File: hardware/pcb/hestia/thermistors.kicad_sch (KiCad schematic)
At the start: 62 parts, among them J10 B2B-ZR, J11 B2B-ZR, J12 B2B-ZR, J13 B2B-ZR, J14 B2B-ZR, J15 B2B-ZR, J16 B2B-ZR, J7 B2B-ZR, J8 B2B-ZR, J9 B2B-ZR, U4 MAX31725MTA+T, U5 MAX31725MTA+T, U6 MAX31725MTA+T, U7 MAX31725MTA+T

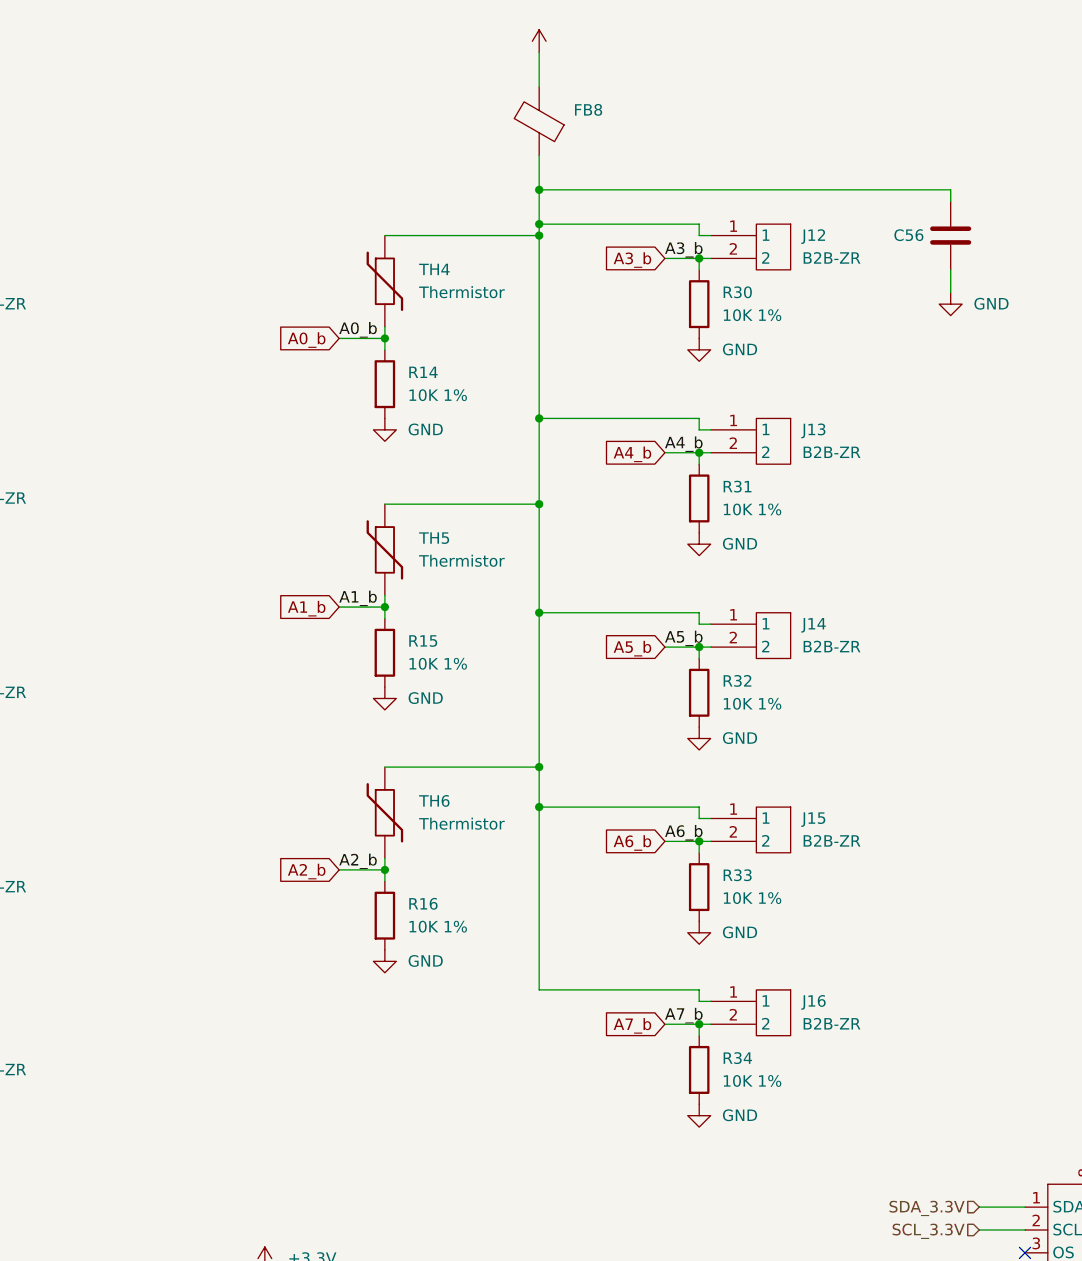
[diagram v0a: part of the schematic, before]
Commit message: add another indicator led. add heater indicator led. add chipbeads to u3 adc input circuits. widen 3.3V trace to accomodate routing for adc and i2c sensors that were on 5V VCC previosuly. untangled most of the i2c signals. move some led traces from uC.
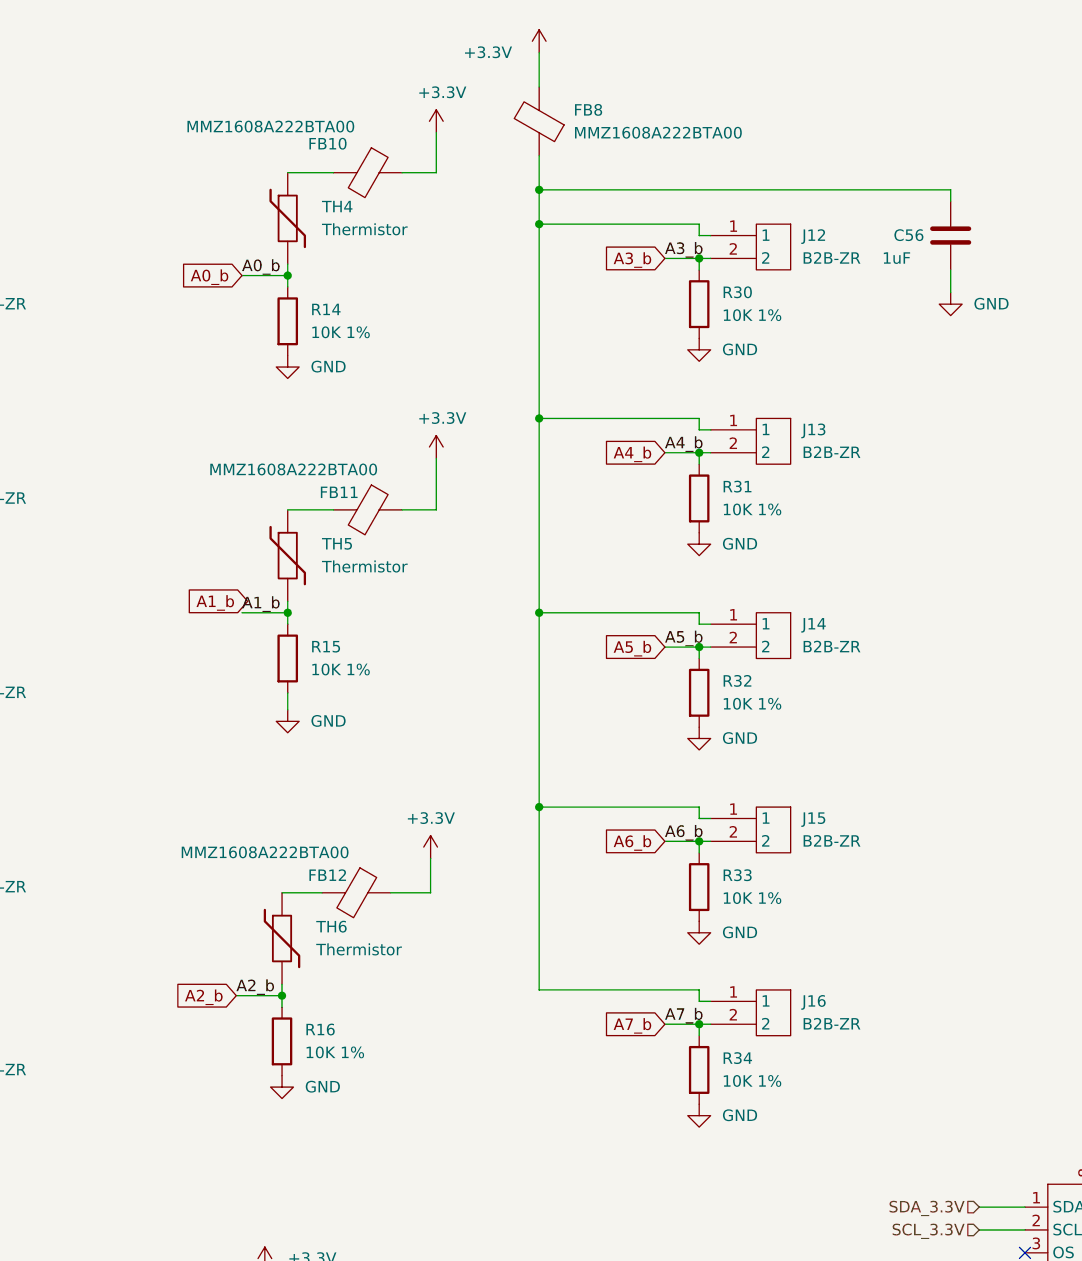
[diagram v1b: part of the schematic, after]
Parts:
- added FB10, FB11, FB12: MMZ1608A222BTA00, Resistor_SMD:R_0603_1608Metric_Pad0.98x0.95mm_HandSolder, symbol Device:FerriteBead
- C56: value (none) -> 1uF; footprint (none) -> Capacitor_SMD:C_0603_1608Metric_Pad1.08x0.95mm_HandSolder
- FB8: value (none) -> MMZ1608A222BTA00; footprint (none) -> Resistor_SMD:R_0603_1608Metric_Pad0.98x0.95mm_HandSolder
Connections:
- net +3V3: now also FB10.1, FB11.1, FB12.1
- net at C56.1, FB8.1, J12.1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: no longer TH4.1, TH5.1, TH6.1
- new net: FB12.2, TH6.1
- new net: FB11.2, TH5.1
- new net: FB10.2, TH4.1
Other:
- moved on the sheet: R14, R15, R16, TH4, TH5, TH6

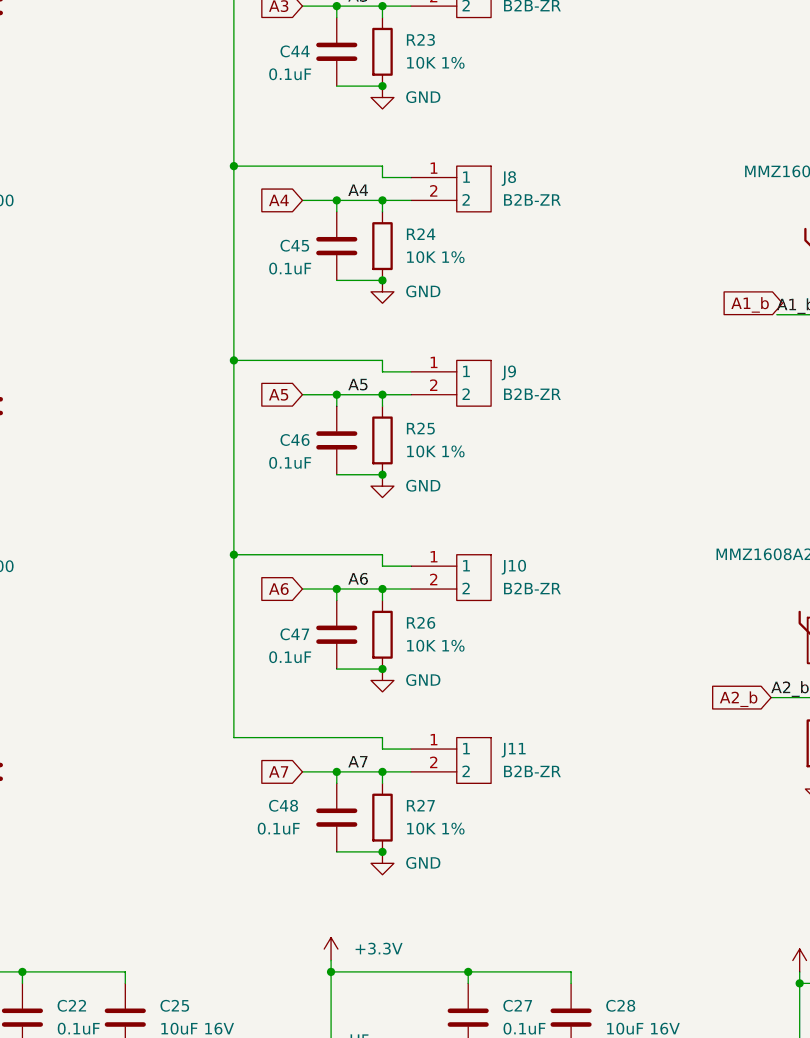
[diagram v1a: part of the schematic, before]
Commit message: removed no longer used thermisters
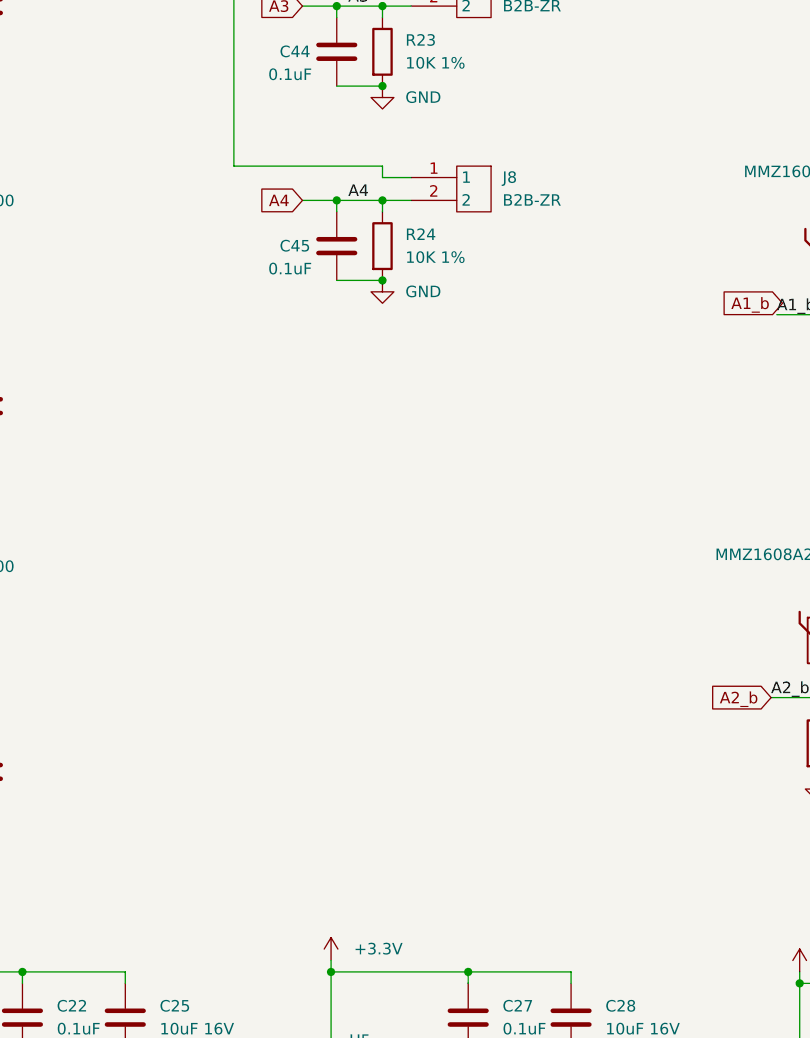
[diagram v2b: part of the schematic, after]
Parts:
- removed C46, C47, C48: 0.1uF, Capacitor_SMD:C_0603_1608Metric_Pad1.08x0.95mm_HandSolder, symbol Device:C
- removed J10, J11, J9: B2B-ZR, Hestia:B2B-ZR(LF)(SN), symbol Hestia:B2B-ZR
- removed R25, R26, R27: 10K 1%, Resistor_SMD:R_0603_1608Metric_Pad0.98x0.95mm_HandSolder, symbol Device:R

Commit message: pcb: add Manufacturer and Type fields for PCBWay BOM
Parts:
- C22, C25, C27, C28, C29, C30, C31, C32, C42, C43, C44, C45, C49, C50, C51, C52, C53, C56, FB10, FB11, FB12, FB4, FB5, FB6, FB7, FB8, R11, R12, R13, R14, R15, R16, R23, R24, R30, R31, R32, R33, R34, TH1, TH2, TH3, TH4, TH5, TH6: Type (none) -> SMD
- U4, U5, U6, U7: Manufacturer (none) -> Maxim; Type (none) -> SMD

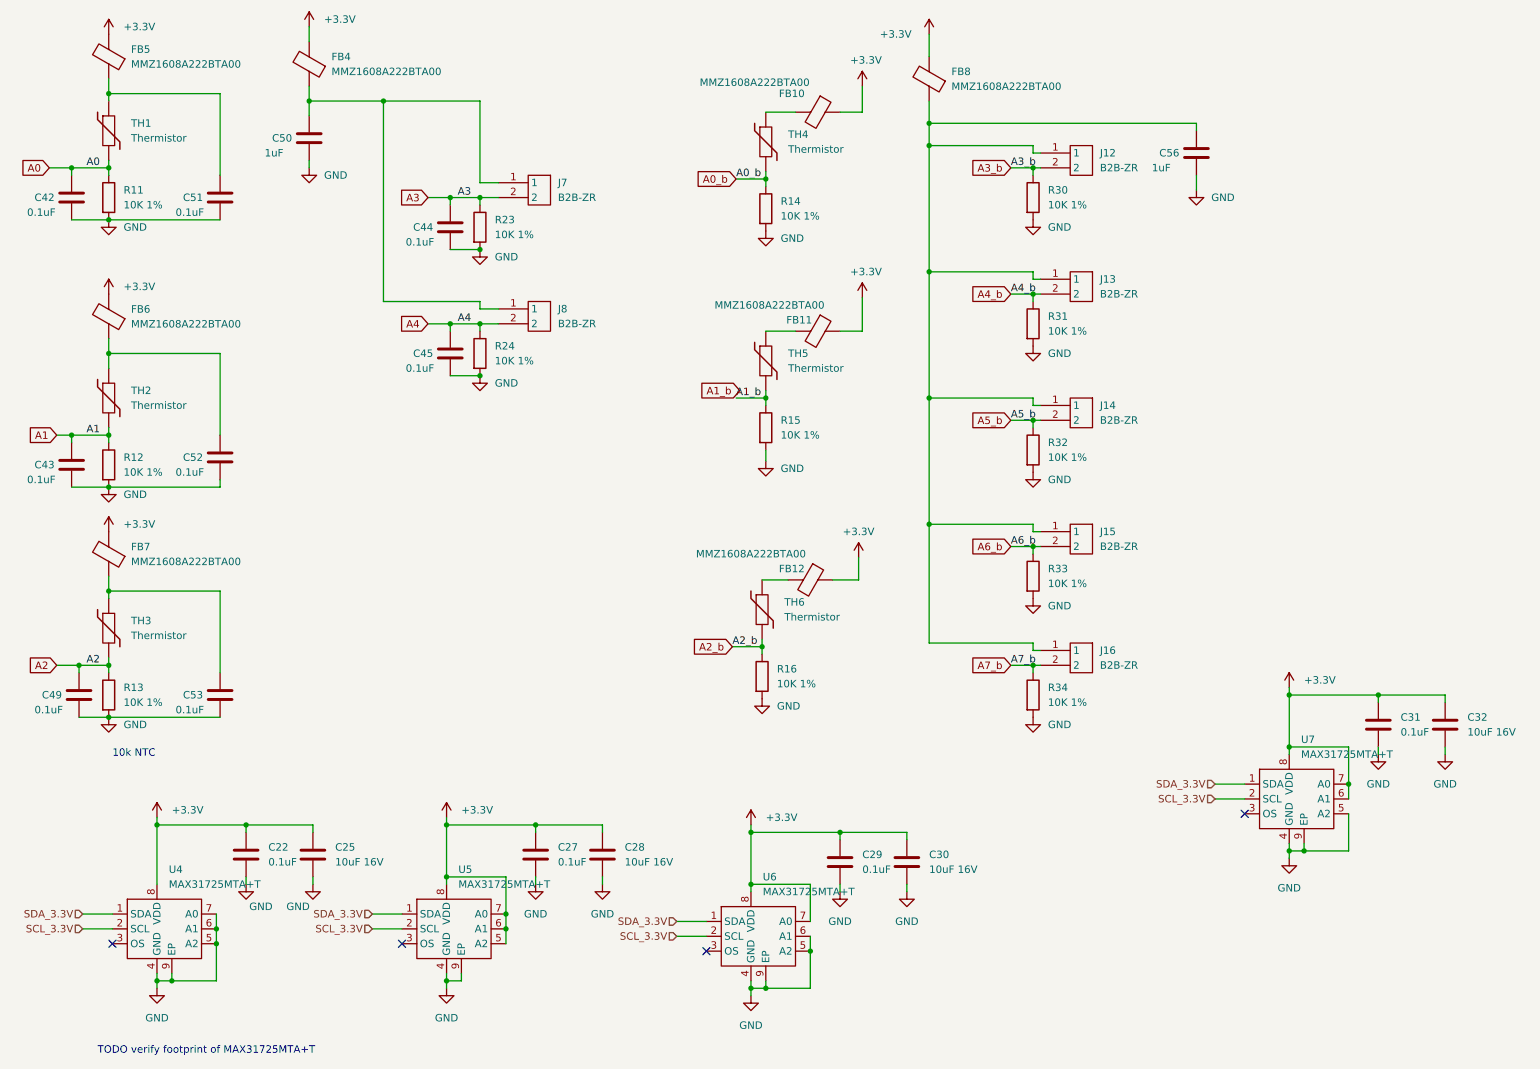
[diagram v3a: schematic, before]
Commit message: added some digikey and mouser part numbers to schematic parts
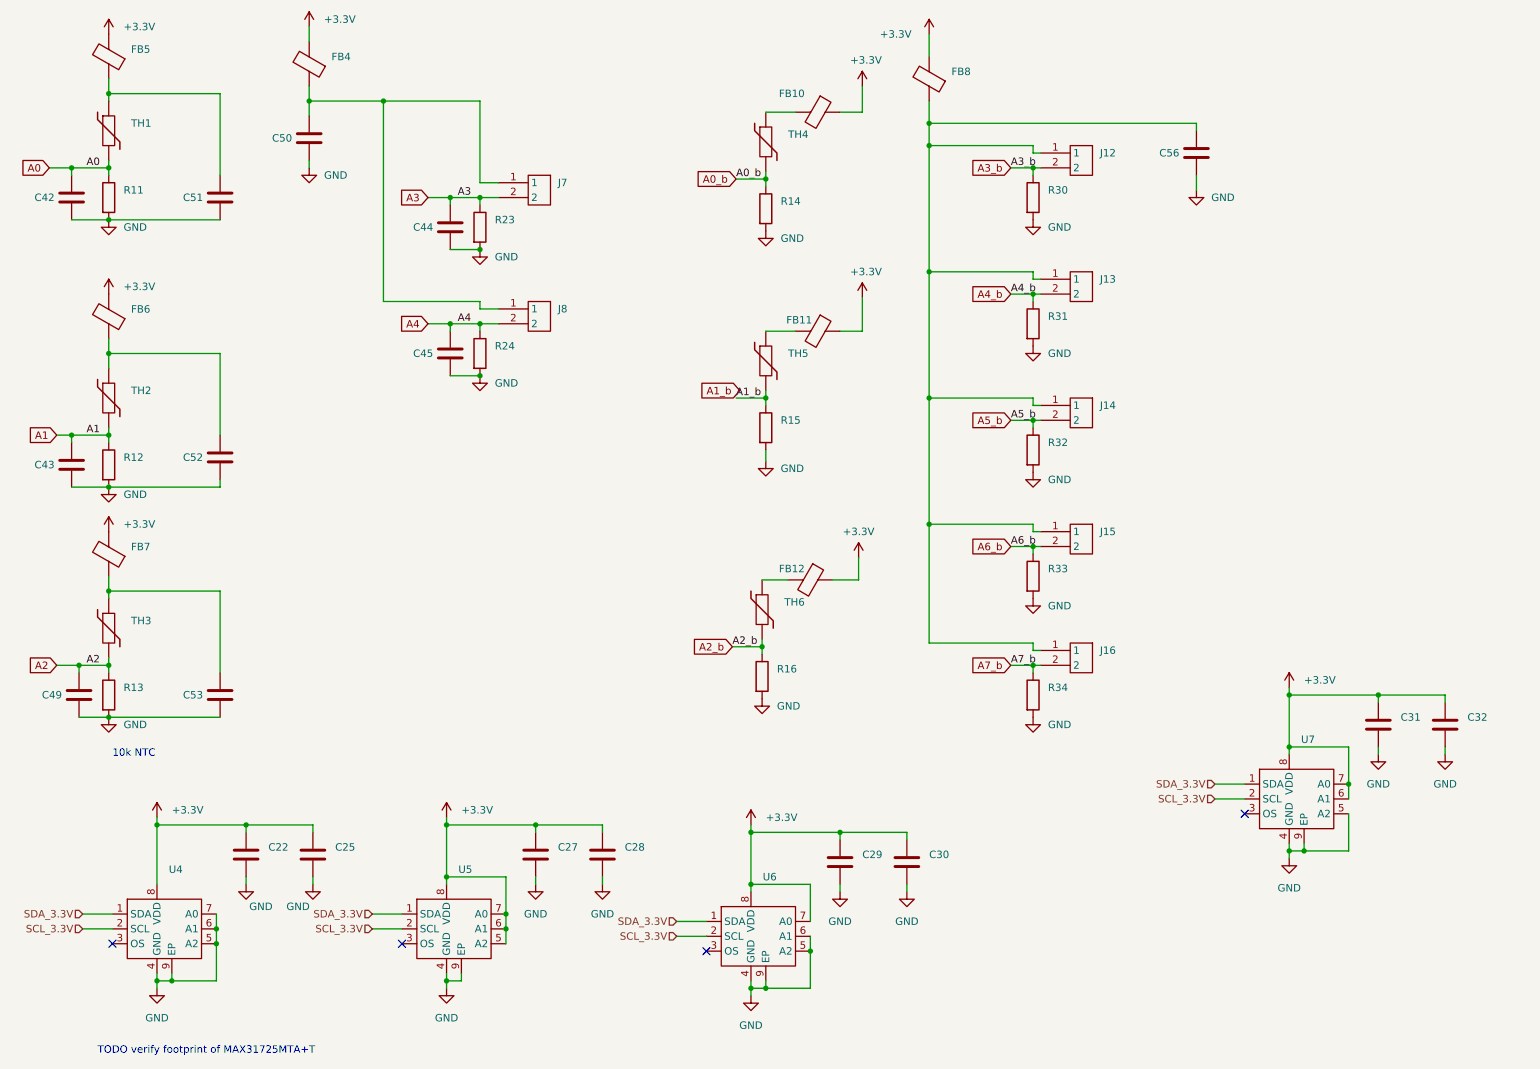
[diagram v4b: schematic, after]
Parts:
- C22, C27, C29, C31, C42, C43, C44, C45, C49, C51, C52, C53: value 0.1uF -> (none); footprint Capacitor_SMD:C_0603_1608Metric_Pad1.08x0.95mm_HandSolder -> (none)
- C25, C28, C30, C32: value 10uF 16V -> (none); footprint Capacitor_SMD:C_0603_1608Metric_Pad1.08x0.95mm_HandSolder -> (none)
- C50, C56: value 1uF -> (none); footprint Capacitor_SMD:C_0603_1608Metric_Pad1.08x0.95mm_HandSolder -> (none)
- FB10, FB11, FB12, FB4, FB5, FB6, FB7, FB8: value MMZ1608A222BTA00 -> (none); footprint Resistor_SMD:R_0603_1608Metric_Pad0.98x0.95mm_HandSolder -> (none); Mouser Part (none) -> 810-MMZ1608A222BTA00
- J12, J13, J14, J15, J16, J7, J8: value B2B-ZR -> (none); footprint Hestia:B2B-ZR(LF)(SN) -> (none)
- R11, R12, R13, R14, R15, R16, R23, R24, R30, R31, R32, R33, R34: value 10K 1% -> (none); footprint Resistor_SMD:R_0603_1608Metric_Pad0.98x0.95mm_HandSolder -> (none)
- TH1, TH2, TH3, TH4, TH5, TH6: value Thermistor -> (none); footprint Resistor_SMD:R_0603_1608Metric_Pad0.98x0.95mm_HandSolder -> (none)
- U4, U5, U6, U7: value MAX31725MTA+T -> (none); footprint Package_DFN_QFN:DFN-8-1EP_3x3mm_P0.65mm_EP1.55x2.4mm -> (none); Digikey Part (none) -> MAX31725MTA+TCT-ND
